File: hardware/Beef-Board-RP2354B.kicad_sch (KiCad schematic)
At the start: 79 parts, among them J1 USB-C DEVICE, J10 VAUX OUT, J11 B1 LEGACY, J12 B2 LEGACY, J13 B3 LEGACY, J14 B4 LEGACY, J15 B5 LEGACY, J16 B6 LEGACY, J17 B7 LEGACY, J18 B8 LEGACY, J19 B9 LEGACY, J2 POWER SELECT, J20 B10 LEGACY, J21 B11 LEGACY, J22 USB COMMON, J3 VAUX 5V INPUT, J31 ENCODER 1, J32 ENCODER 2, J33 AE1 0-5V, J34 AE2 0-5V, J4 USB-C AUX POWER, J40 TT RGB, J41 CENTER BAR RGB, J42 UART A 3V3, J43 UART B 3V3, J5 ENC1 A, J6 ENC1 B, J60 BOOTSEL HEADER, J61 RESET HEADER, J7 ENC2 A, J8 ENC2 B, J9 VAUX OUT, Q1 2N7002, Q10 2N7002, Q11 2N7002, Q2 2N7002, Q3 2N7002, Q4 2N7002, Q5 2N7002, Q6 2N7002, Q7 2N7002, Q8 2N7002, Q9 2N7002, SW2 BOOTSEL, U1 RP2354B, U2 USBLC6-2SC6, U3 AP2112K-3.3, Y1 12MHz CL=10pF

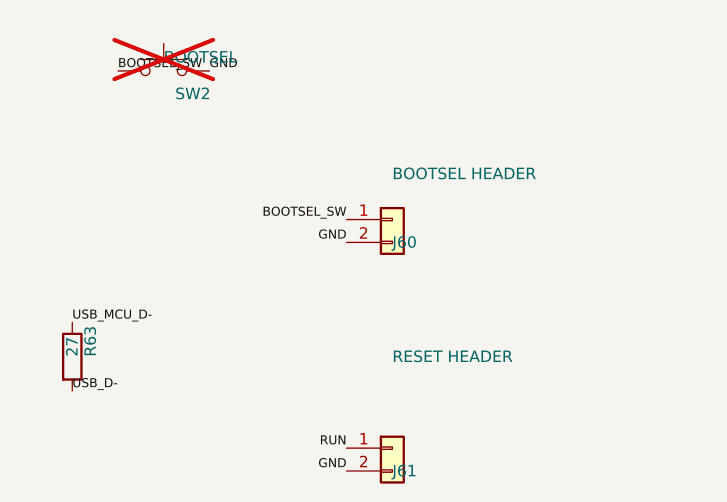
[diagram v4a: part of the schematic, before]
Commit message: Align schematic BOM and flashing guides with current PCB
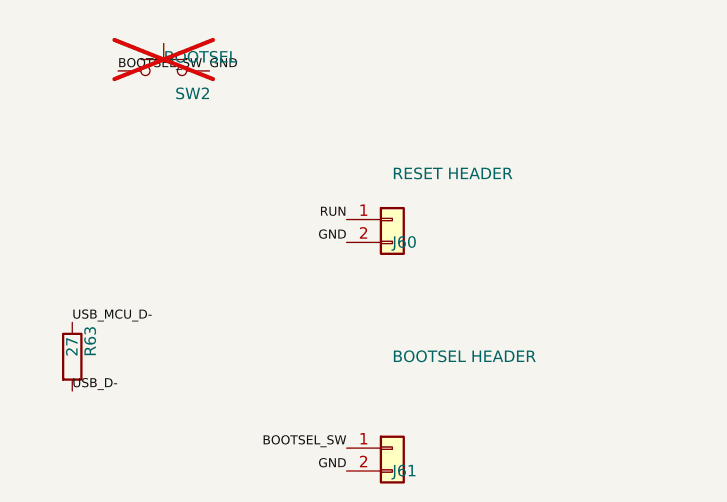
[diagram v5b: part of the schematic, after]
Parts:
- J60: value BOOTSEL HEADER -> RESET HEADER
- J61: value RESET HEADER -> BOOTSEL HEADER
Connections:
- net BOOTSEL_SW: now also J61.1 (Pin_1); no longer J60.1 (Pin_1)
- net RUN: now also J60.1 (Pin_1); no longer J61.1 (Pin_1)

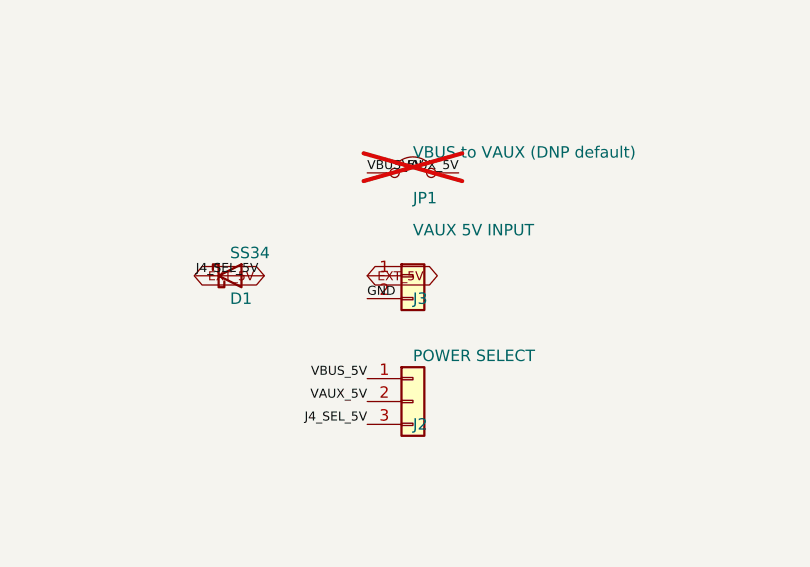
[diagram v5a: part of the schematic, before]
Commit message: Align J3 polarity and docs with revised PCB
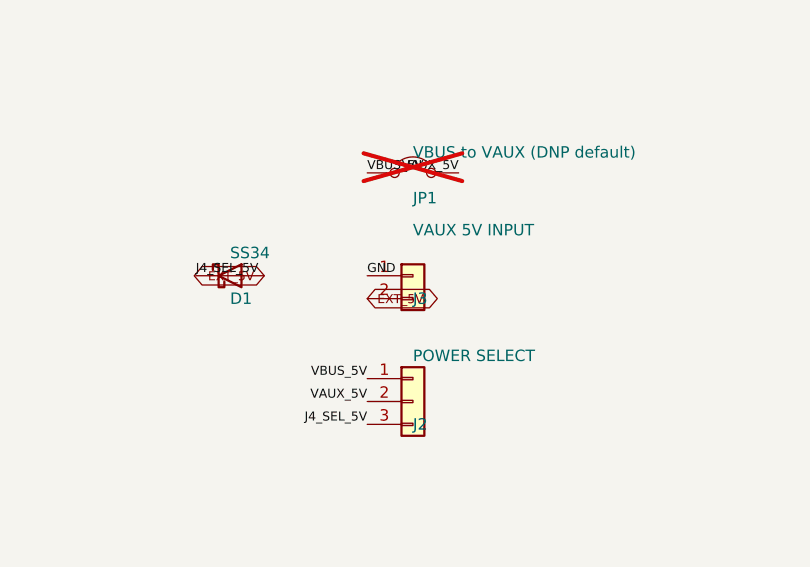
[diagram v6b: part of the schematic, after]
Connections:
- net EXT_5V: now also J3.2 (Pin_2); no longer J3.1 (Pin_1)
- net GND: now also J3.1 (Pin_1); no longer J3.2 (Pin_2)

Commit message: hardware: adopt corrected crystal routing and JLCPCB assembly settings
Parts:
- J11, J12, J13, J14, J15, J16, J17, J18, J19, J20, J21, J31, J32, J42, J43, J60, J61: now not fitted
- J3: footprint TerminalBlock_Phoenix:TerminalBlock_Phoenix_MKDS-1,5-2_1x02_P5.00mm_Horizontal -> Connector_JST:JST_PH_B2B-PH-K_1x02_P2.00mm_Vertical
- J33, J34: footprint Connector_JST:JST_XH_B3B-XH-A_1x03_P2.50mm_Vertical -> Connector_JST:JST_PH_B3B-PH-K_1x03_P2.00mm_Vertical
- JP1, SW2: now fitted
- Y1: symbol Device:Crystal -> Device:Crystal_GND24
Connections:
- net GND: now also Y1.2 (G), Y1.4 (G)
- net HSE_OUT: now also Y1.3; no longer Y1.2
